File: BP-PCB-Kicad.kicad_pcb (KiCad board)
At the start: 2 copper layers, 98 x 120.7 mm, 67 parts, among them IC1 LMT84DCKT, J1 A3C-50DA-2DSA_71_, J10 A3C-50DA-2DSA_71_, J13 Conn_01x20, J14 Conn_01x20, J15 DF14-30P-1.25H_35_, J16 A3C-50DA-2DSA_71_, J17 A3C-4DA-2DSA_71_, J18 A3C-4DA-2DSA_71_, J19 Molex 55460-0272, J2 A3C-50DA-2DSA_71_, J21 Molex 55460-0272, J22 Molex 55460-0272, J23 DF14-15P-1.25H52, J3 A3C-4DA-2DSA_71_, J4 A3C-4DA-2DSA_71_, J7 DF14-15P-1.25H52, J8 DF14-15P-1.25H52, J9 A3C-50DA-2DSA_71_, Q1 SSM6K514NU,LF, Q2 SSM6K514NU,LF, Q3 SSM6K514NU,LF, Q4 SSM6K514NU,LF, Q5 SSM6K514NU,LF, Q6 SSM6K514NU,LF, U1 LTC4361CTS8-2TRMPBF, U2 LTC4361CTS8-2TRMPBF, U3 SN74CB3Q3257DBQR, U4 LTC4380IDD-4-PBF, U5 SN74CB3Q3257DBQR, U6 LTC4380IDD-4-PBF

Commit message: PCB layout is syncronized with schematic
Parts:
- removed U4: LTC4380IDD-4-PBF, Custom-Footprints:LTC4380IDD-4#PBF
- added J5: Conn_01x03_Pin, Connector_PinHeader_2.54mm:PinHeader_1x03_P2.54mm_Vertical, F.Cu at (35.0, 113.4)
- added R20: 2.5 Ohm, Resistor_SMD:R_0805_2012Metric, F.Cu at (36.5, 67.5)
- added R21: 500, Resistor_SMD:R_0805_2012Metric, F.Cu at (39.3, 114.8)
- added U7: LTC4389IMS-4#PBF, Custom-Footprints:LTC4380IMS-4#PBF, F.Cu at (39.0, 45.8)
- R10, R9: value R0603EIA (1508METRIC) -> 25m
- R16, R17: value R0603EIA (1508METRIC) -> 25m Ohm
- R18: value 1k -> 5 Ohm
- R19: value 1k -> 500
- R3: value 1.67 Ohm -> 2.5 Ohm
- U6: value LTC4380IDD-4-PBF -> LTC4389IMS-4#PBF; footprint Custom-Footprints:LTC4380IDD-4#PBF -> Custom-Footprints:LTC4380IMS-4#PBF
- moved R19 129.1 mm to (39.3, 119.0), turned to -90 degrees
- moved C6 124.1 mm to (32.7, 63.9), turned to -90 degrees
- moved R15 120.4 mm to (28.2, 40.3)
- moved C17 116.6 mm to (39.7, 123.7), turned to 90 degrees
- moved C15 112.1 mm to (27.2, 50.3)
- moved R13 111.5 mm to (32.2, 50.3)
- moved C14 111.2 mm to (28.2, 45.3)
- moved R11 110.7 mm to (33.2, 41.3)
- moved Q6 110.0 mm to (36.5, 50.3)
- moved C4 109.1 mm to (41.6, 62.1)
- moved C7 107.8 mm to (64.0, 94.0)
- moved R17 107.3 mm to (45.2, 43.6)
- moved R12 106.1 mm to (38.2, 40.3)
- moved C13 106.0 mm to (33.2, 46.3)
- moved R14 105.3 mm to (43.1, 40.3)
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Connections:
- net MUX-CCB_UART (CCB_to_MainPIC) renamed MUX-CCB_UART (FPGA_to_MainPIC)
- net MUX-CCB_UART (MainPIC_to_CCB) renamed MUX-CCB_UART (MainPIC_to_FPGA)
- net OBC-MUX_UART (CCB/ThermalPIC_to_MainPIC) renamed OBC-MUX_UART (FPGA/ThermalPIC_to_MainPIC)
- net OBC-MUX_UART (MainPIC_to_CCB/ThermalPIC) renamed OBC-MUX_UART (MainPIC_to_FPGA/ThermalPIC)
- net UART (ADCS_to_CCB) renamed Earth_Sensor_UART (ADCS_to_RPi)
- net UART (CCB_to_ADCS) renamed Earth_Sensor_UART (RPi_to_ADCS)
- C1 pad 2: GND -> GND_SYS
- C10 pad 2: GND -> GND_SYS
- C11 pad 2: GND -> GND_SYS
- C12 pad 2: GND -> GND_SYS
- C13 pad 1: Net-(U6-VCC) -> Net-(U7-VCC)
- C13 pad 2: GND -> GND_SYS
- C14 pad 1: Net-(U6-TMR) -> Net-(U7-TMR)
- C14 pad 2: GND -> GND_SYS
- C15 pad 2: GND -> GND_SYS
- C16 pad 2: GND -> GND_SYS
- C17 pad 2: GND -> GND_SYS
- C2 pad 1: SUP_3V3_1 -> TEMP_3v3_MX
- C2 pad 2: GND -> GND_SYS
- C3 pad 2: GND -> GND_SYS
- C4 pad 2: GND -> GND_SYS
- C5 pad 2: GND -> GND_SYS
- C6 pad 2: GND -> GND_SYS
- C7 pad 2: GND -> GND_SYS
- C8 pad 1: Net-(U4-VCC) -> Net-(U6-VCC)
- C8 pad 2: GND -> GND_SYS
- C9 pad 1: Net-(U4-TMR) -> Net-(U6-TMR)
- C9 pad 2: GND -> GND_SYS
- IC1 pad 1: GND -> GND_SYS
- IC1 pad 2: GND -> GND_SYS
- IC1 pad 4: SUP_3V3_1 -> TEMP_3v3_MX
- IC1 pad 5: GND -> GND_SYS
- J1 pad 15: SUP_5V_1 -> unconnected-(J1-Pad15)
- J1 pad 16: SUP_5V_1 -> unconnected-(J1-Pad16)
- J1 pad 25: SUP_5V_2 -> unconnected-(J1-Pad25)
- J1 pad 26: SUP_5V_2 -> unconnected-(J1-Pad26)
- J1 pad 35: SUP_UNREG_2 -> unconnected-(J1-Pad35)
- J1 pad 36: SUP_UNREG_2 -> unconnected-(J1-Pad36)
- J10 pad 25: Thruster-1 -> Thruster_1
- J10 pad 26: Thruster-2 -> Thruster_2
- J10 pad 35: Thurster_3 -> Thruster_3
- J13 pad 10: unconnected-(J13-Pin_10-Pad10) -> E-MGM_3v3
- J13 pad 11: unconnected-(J13-Pin_11-Pad11) -> E-MGM_SDA
- J13 pad 12: unconnected-(J13-Pin_12-Pad12) -> E-MGM_SCL
- J13 pad 2: TEMP_-X -> GND_SYS
- J13 pad 3: TEMP_3v3_MX -> TEMP_-X
- J13 pad 4: unconnected-(J13-Pin_4-Pad4) -> TEMP_3v3_MX
- J14 pad 5: unconnected-(J14-Pin_5-Pad5) -> TEMP_-Z
- J14 pad 8: unconnected-(J14-Pin_8-Pad8) -> Sunsensor_-Z1
- J14 pad 9: unconnected-(J14-Pin_9-Pad9) -> Sunsensor_-Z2
- J15 pad 1: OBC-CCB DIO ON/OFF (MainPIC_to_CCB) -> OBC-CCB_DIO_ON/OFF (MainPIC_to_CCB)
- J15 pad 25: SUP_12V0 -> SUP_12V
- J15 pad 26: SUP_12V0 -> SUP_12V
- J2 pad 11: POWERSC_-Z (nc) -> unconnected-(J2-Pad11)
- J2 pad 12: POWERSC_-Z (nc) -> unconnected-(J2-Pad12)
- J2 pad 33: POWERSC_-X_1 -> POWERSC_-X1
- J2 pad 34: POWERSC_-X_1 -> POWERSC_-X1
- J2 pad 45: Sunsensor -Y -> Sunsensor_-Y
- J2 pad 47: POWERSC_-X_2 -> POWERSC_-X2
- J2 pad 48: POWERSC_-X_2 -> POWERSC_-X2
- J23 pad 5: SUP_3V3 -> SUP_3V3_1
- J3 pad 3: SUP_UNREG_3 -> SUP_UNREG_1
- J3 pad 4: SUP_UNREG_3 -> SUP_UNREG_1
- J9 pad 12: Sunsensor_-Z -> Sunsensor_-Z1
- J9 pad 21: unconnected-(J9-Pad21) -> Sunsensor_-Z2
- J9 pad 33: unconnected-(J9-Pad33) -> E-MGM_3v3
- J9 pad 37: unconnected-(J9-Pad37) -> E-MGM_SDA
- J9 pad 38: unconnected-(J9-Pad38) -> E-MGM_SCL
- J9 pad 46: unconnected-(J9-Pad46) -> OBC-ADCS_DIO_ON/OFF (MainPIC_to_ADCS)
- J9 pad 6: OBC-ADCS_DIO_ON/OFF (MainPIC_to_ADCS) -> unconnected-(J9-Pad6)
- R11 pad 2: Net-(U6-VCC) -> Net-(U7-VCC)
- R12 pad 2: Net-(U6-DRN) -> Net-(U7-DRN)
- R13 pad 2: GND -> GND_SYS
- R14 pad 1: Net-(U6-GATE) -> Net-(U7-GATE)
- R15 pad 1: Net-(U6-GATE) -> Net-(U7-GATE)
- R18 pad 1: SUP_UNREG_2 -> SUP_3V3_1
- R18 pad 2: SBAND_TX_TEMP1 (sensor + terminal)  -> Net-(Q1-D_1)
- R19 pad 1: GND -> GND_SYS
- R4 pad 2: Net-(U4-VCC) -> Net-(U6-VCC)
- R5 pad 2: Net-(U4-DRN) -> Net-(U6-DRN)
- R6 pad 2: GND -> GND_SYS
- R7 pad 1: Net-(U4-GATE) -> Net-(U6-GATE)
- R8 pad 1: Net-(U4-GATE) -> Net-(U6-GATE)
- U1 pad 1: GND -> GND_SYS
- U1 pad 4: GND -> GND_SYS
- U2 pad 1: GND -> GND_SYS
- U2 pad 4: GND -> GND_SYS
- U3 pad 15: GND -> GND_SYS
- U3 pad 8: GND -> GND_SYS
- U5 pad 12: GND -> GND_SYS
- U5 pad 15: GND -> GND_SYS
- U5 pad 8: GND -> GND_SYS
- U5 pad 9: GND -> GND_SYS
- U6 pad 4: Net-(Q5-D_1) -> Net-(Q3-D_1)
- U6 pad 5:  V_IN (Unreg2 OCP to S-band RX) ->  V_IN (Unreg2 OCP to S-band TX)
- U6 pad 6: GND -> GND_SYS
- U6 pad 8: GND -> GND_SYS
- U6 pad 9: DIO_S-Band_RX_ON/OFF -> DIO_S-Band_TX_ON/OFF
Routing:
- net SUP_UNREG_1: track 0.00 -> 126.8 mm
- net SUP_5V_2: track 0.00 -> 107.2 mm
- net SUP_3V3_1: track 0.00 -> 106.5 mm
- net GND_SYS: track 0.00 -> 43.0 mm, vias 0 -> 2
- net SUP_12V: track 0.00 -> 16.4 mm
- net RAW_POWER: track 0.00 -> 16.4 mm
- net PGD: track 0.00 -> 5.99 mm
- added copper zone on In1.Cu, net GND_SYS
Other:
- copper layers 2 -> 4
- board text added: "+X OCP"
- board text added: "-X OCP"
- board text added: "BPB Temp Sensor"
- board text added: "S-b TX Temp Cir"

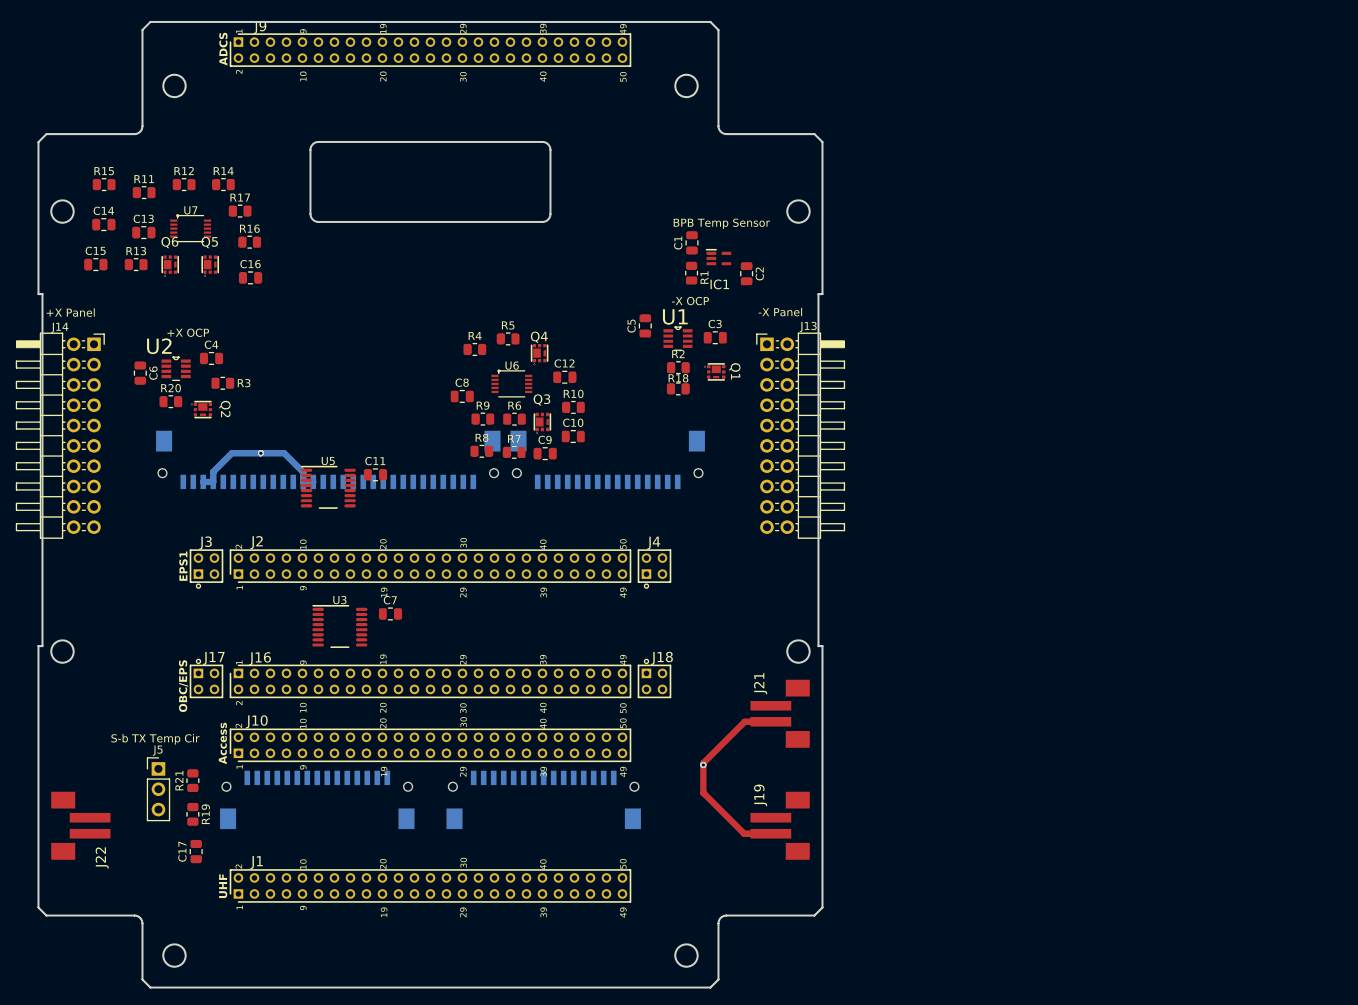
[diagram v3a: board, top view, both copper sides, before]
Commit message: Microelectronic components placed onto the back of BPB
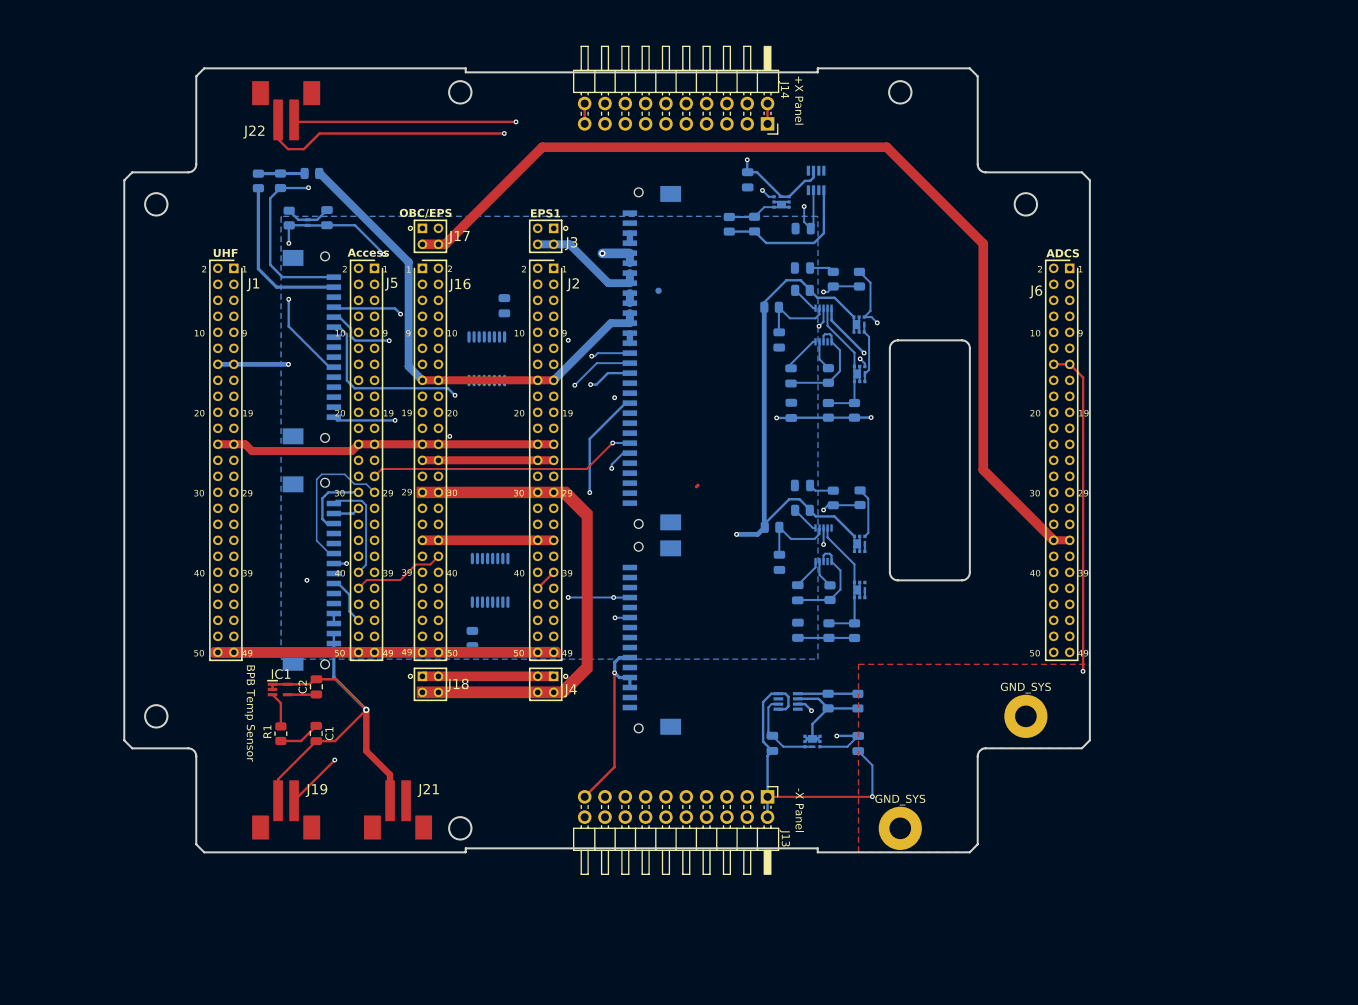
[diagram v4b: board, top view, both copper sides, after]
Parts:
- removed J10: A3C-50DA-2DSA_71_, Custom-Footprints:Hirose_A3C-50DA-2DSC(71)
- removed J9: A3C-50DA-2DSA_71_, Custom-Footprints:Hirose_A3C-50DA-2DSC(71)_Mirrored
- added D1: BZT52C3V6LP-7, Custom-Footprints:DIO_BZT52C3V6LP-7, B.Cu at (53.6, 45.1)
- added GND_SYS: MountingHole_2.7mm_Pad, MountingHole:MountingHole_2.7mm_Pad, F.Cu at (143.4, 106.8)
- added GND_SYS: MountingHole_2.7mm_Pad, MountingHole:MountingHole_2.7mm_Pad, F.Cu at (127.7, 120.8)
- added J6: A3C-50DA-2DSA_71_, Custom-Footprints:Hirose_A3C-50DA-2DSC(71)_Mirrored, F.Cu at (148.9, 50.8)
- added R22: 0, Resistor_SMD:R_0805_2012Metric, B.Cu at (50.2, 39.9)
- added R23: 0, Resistor_SMD:R_0805_2012Metric, B.Cu at (54.2, 38.9)
- C10, C11, C12, C13, C14, C15, C16, C17, C3, C4, C5, C6, C7, C8, C9, Q1, Q2, Q3, Q4, Q5, Q6, R10, R11, R12, R13, R14, R15, R16, R17, R18, R19, R2, R20, R21, R3, R4, R5, R6, R7, R8, R9, U1, U2, U3, U5, U6, U7: moved to B.Cu
- J1, J2: footprint Custom-Footprints:Hirose_A3C-50DA-2DSC(71) -> Custom-Footprints:Hirose_A3C-50DA-2DSC(71)_Mirrored
- J16: footprint Custom-Footprints:Hirose_A3C-50DA-2DSC(71)_Mirrored -> Custom-Footprints:Hirose_A3C-50DA-2DSC(71)
- J17, J18: footprint Custom-Footprints:Hirose_A3C-4DA-2DSA(71)_Mirrored -> Custom-Footprints:Hirose_A3C-4DA-2DSA(71)
- J3, J4: footprint Custom-Footprints:Hirose_A3C-4DA-2DSA(71) -> Custom-Footprints:Hirose_A3C-4DA-2DSA(71)_Mirrored
- J5: value Conn_01x03_Pin -> A3C-50DA-2DSA_71_; footprint Connector_PinHeader_2.54mm:PinHeader_1x03_P2.54mm_Vertical -> Custom-Footprints:Hirose_A3C-50DA-2DSC(71)_Mirrored
- moved R15 102.3 mm to (122.7, 79.5), turned to 90 degrees
- moved C14 98.2 mm to (114.9, 91.3), turned to -90 degrees
- moved R13 95.9 mm to (118.9, 91.3), turned to -90 degrees
- moved R17 93.0 mm to (122.0, 96.1), turned to -90 degrees
- moved Q6 93.0 mm to (122.7, 85.2)
- moved C15 92.5 mm to (115.5, 77.9), turned to 180 degrees
- moved J22 92.3 mm to (50.0, 32.2), turned to 180 degrees
- moved Q5 90.8 mm to (122.7, 91.0)
- moved C13 89.5 mm to (112.6, 87.5), turned to -90 degrees
- moved R11 88.9 mm to (111.7, 83.2)
- moved J14 88.6 mm to (111.1, 32.7), turned to -90 degrees
- moved U7 88.4 mm to (118.1, 85.3), turned to -90 degrees
- moved R12 87.4 mm to (115.5, 81.0), turned to 180 degrees
- moved R16 87.2 mm to (118.8, 96.1), turned to -90 degrees
- moved R14 85.7 mm to (119.3, 79.5), turned to 90 degrees
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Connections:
- J22 pad 2: GND_SYS -> GND_BAT
- J5 pad 1:  V_IN (Unreg2 OCP to S-band TX) -> PGC
- J5 pad 2: Net-(J5-Pin_2) -> PGD
- J5 pad 3: SUP_5V_1 -> MCLR_EpsPIC
- R21 pad 1: Net-(J5-Pin_2) -> Net-(R21-Pad1)
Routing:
- net GND_SYS: track 43.0 -> 213.5 mm, vias 2 -> 5
- net  V_IN (Unreg2 OCP to S-band TX): track 0.00 -> 132.1 mm, vias 0 -> 4
- net SUP_UNREG_3: track 0.00 -> 122.9 mm
- net SUP_UNREG_2: track 0.00 -> 109.4 mm, vias 0 -> 1
- net DEP_SW4: track 0.00 -> 92.6 mm, vias 0 -> 1
- net SUP_5V_2: track 107.2 -> 17.7 mm
- net S-band_TX_Analog_Temperature: track 0.00 -> 82.4 mm, vias 0 -> 3
- net DIO_HW_Reset: track 0.00 -> 64.5 mm, vias 0 -> 3
- net GND_BAT: track 0.00 -> 63.3 mm, vias 0 -> 1
- net DIO_Thruster_Active: track 0.00 -> 62.8 mm, vias 0 -> 2
- net SUP_5V_1: track 0.00 -> 61.4 mm
- net SUP_12V: track 16.4 -> 76.5 mm, vias 0 -> 1
- net SUP_3V3_1: track 106.5 -> 47.2 mm
- net OBC-SBAND_TX_RTS (Sband_TX_to_ComPic): track 0.00 -> 53.0 mm, vias 0 -> 1
- net PGC: track 0.00 -> 49.6 mm, vias 0 -> 1
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- added copper zone on B.Cu, net GND_SYS
- added copper zone on F.Cu, net GND_SYS
- removed copper zone on In1.Cu, net GND_SYS
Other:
- board size 98 x 120.7 mm -> 120.7 x 98 mm
- board text added: "S-b RX OCP"
- board text added: "S-b TX OCP"

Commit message: Routing traces of panels
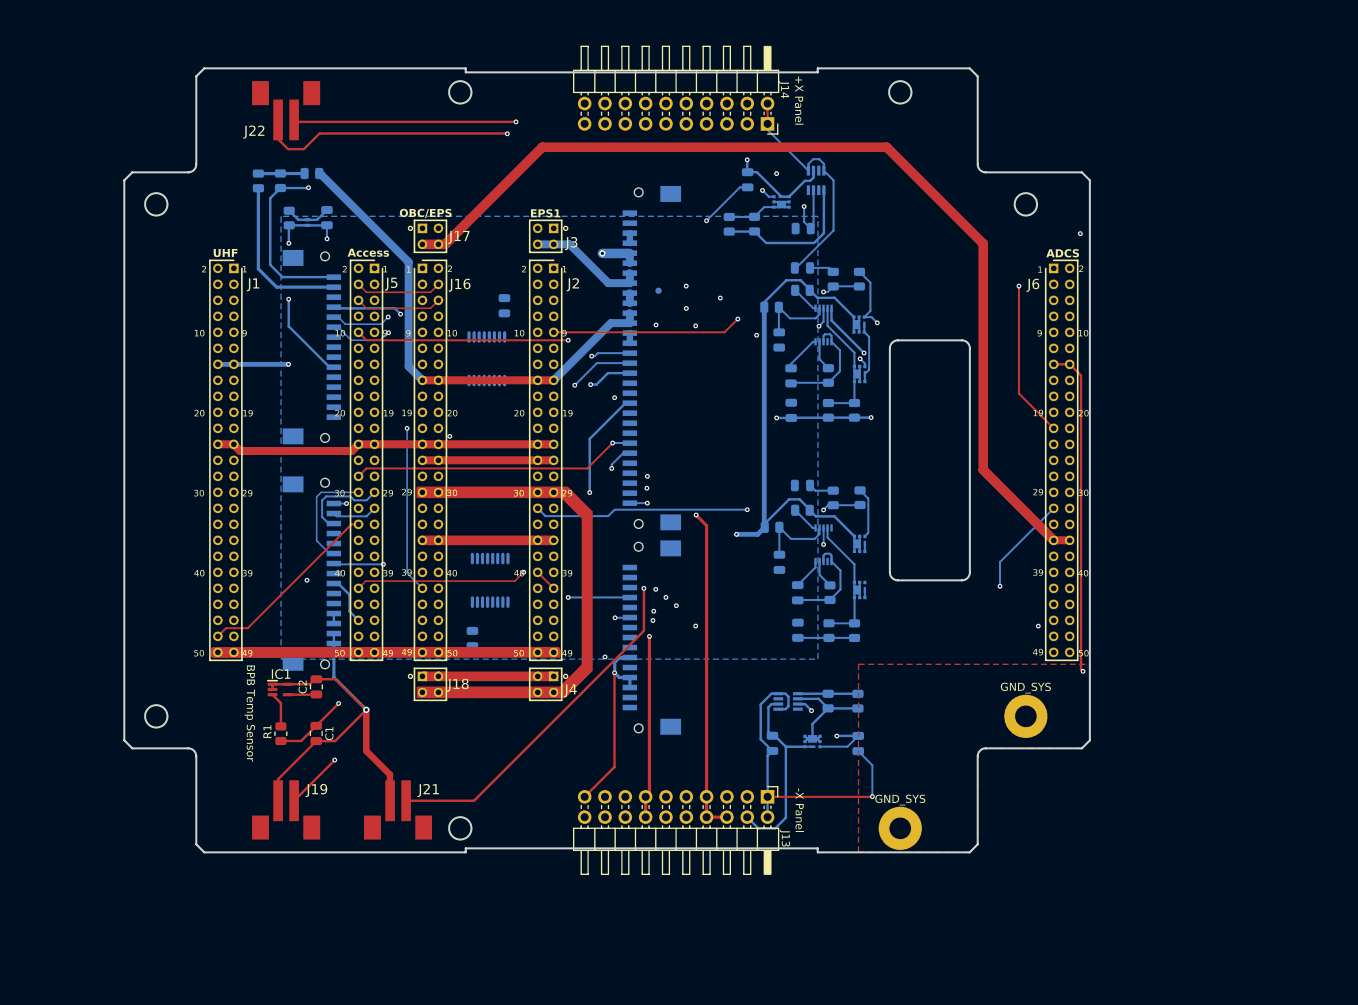
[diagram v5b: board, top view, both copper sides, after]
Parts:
- J6: footprint Custom-Footprints:Hirose_A3C-50DA-2DSC(71)_Mirrored -> Custom-Footprints:Hirose_A3C-50DA-2DSC(71)
- moved J6 2.00 mm to (146.9, 50.8)
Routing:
- net Sunsensor_-X: track 0.00 -> 109.4 mm, vias 0 -> 1
- net E-MGM_3v3: track 0.00 -> 94.6 mm, vias 0 -> 2
- net UART (GPS_to_ADCS): track 0.00 -> 93.4 mm, vias 0 -> 1
- net UART (ADCS_to_GPS): track 0.00 -> 87.8 mm, vias 0 -> 2
- net Sunsensor_-Z2: track 0.00 -> 81.5 mm, vias 0 -> 2
- net GPS_1PPS: track 0.00 -> 79.5 mm, vias 0 -> 1
- net E-MGM_SCL: track 0.00 -> 79.5 mm, vias 0 -> 1
- net E-MGM_SDA: track 0.00 -> 75.5 mm, vias 0 -> 1
- net GPS_3v3: track 0.00 -> 75.0 mm, vias 0 -> 1
- net Sunsensor_+Y: track 0.00 -> 73.4 mm, vias 0 -> 1
- net Sunsensor_-Z1: track 0.00 -> 69.5 mm, vias 0 -> 1
- net Sunsensor_+X: track 0.00 -> 69.2 mm
- net POWERSC_+X: track 0.00 -> 68.0 mm, vias 0 -> 1
- net TEMP_-X: track 0.00 -> 62.8 mm, vias 0 -> 1
- net Sunsensor_+Z: track 0.00 -> 62.4 mm
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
